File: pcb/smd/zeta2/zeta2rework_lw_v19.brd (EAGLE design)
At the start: 80.3 x 45.7 mm, 94 parts, among them IC1 MAX6520, U5 DS18B20U+

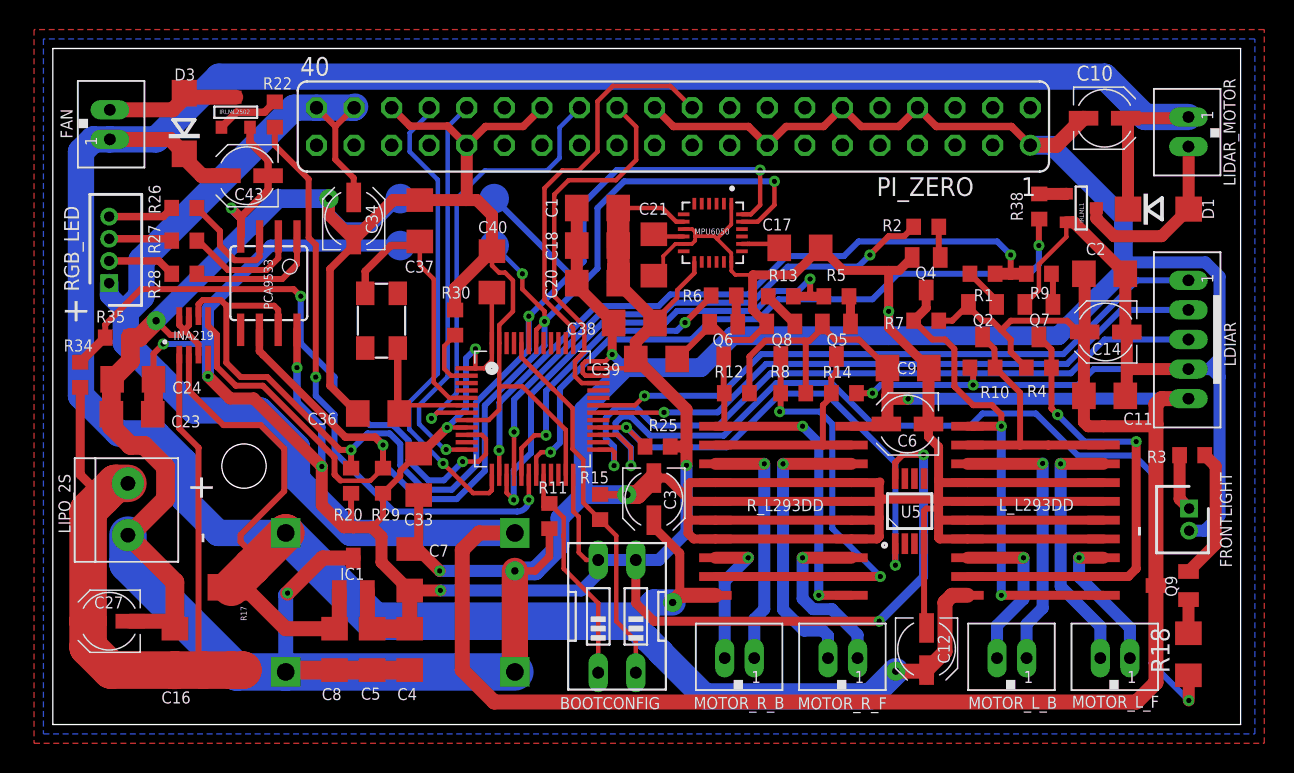
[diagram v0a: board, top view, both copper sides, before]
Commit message: using ph for leds again
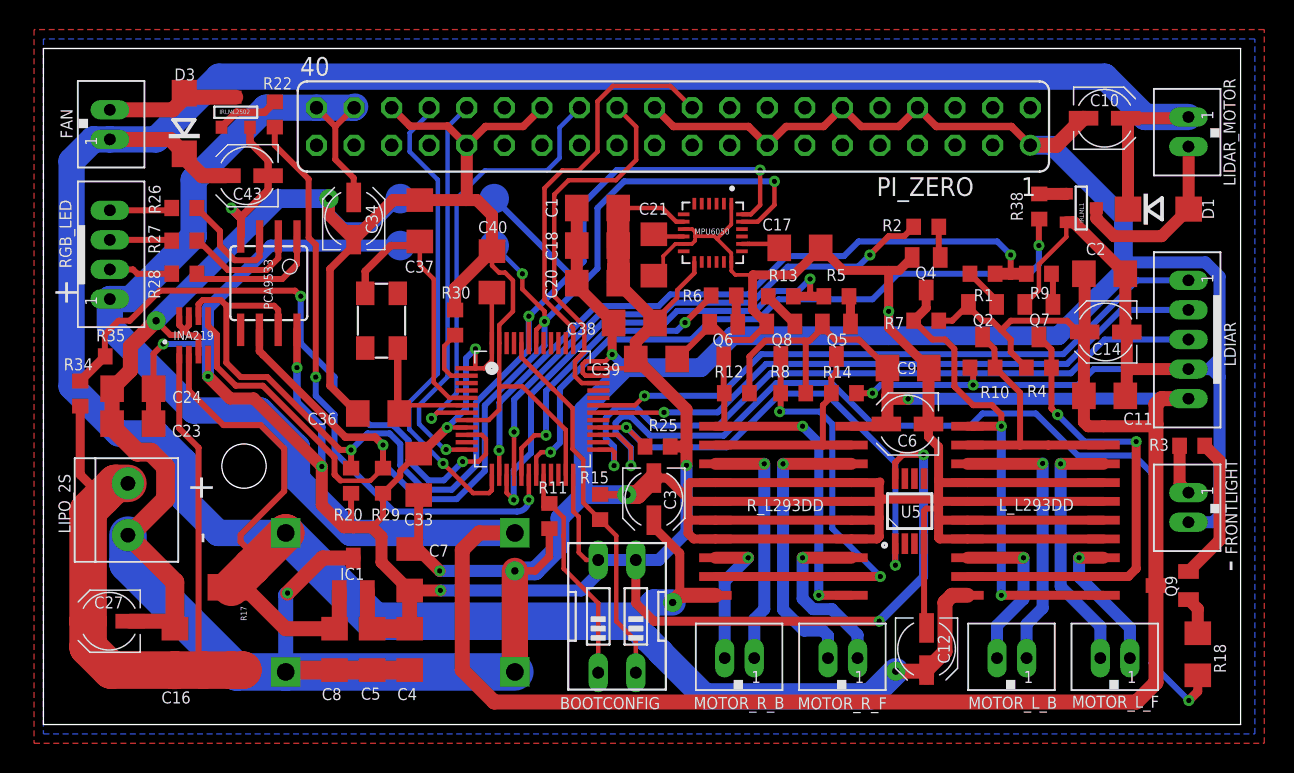
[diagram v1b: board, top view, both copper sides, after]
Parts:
- FRONTLIGHT: value B2B-ZR(LF)(SN) -> JST-PH_2-PIN_HEADER; device B2B-ZR(LF)(SN):SHDR2W50P0X150_1X2_450X350X450 -> srg:JST_B2B-PH_HEADER
- RGB_LED: value B4B-ZR(LF)(SN) -> JST-PH_4-PIN_HEADER; device B4B-ZR(LF)(SN):SHDR4W50P0X150_1X4_750X350X450 -> srg:JST_B4B-PH_HEADER
- moved RGB_LED 1.91 mm to (3.81, 38.7)
- moved R34 1.27 mm to (1.85, 29.4)
- moved R35 1.27 mm to (4.39, 31.9)
- moved C23 0.64 mm to (5.41, 27.3)
- moved R18 0.64 mm to (77.4, 11.7)
- moved C24 0.64 mm to (5.41, 29.7)
- moved R3 0.64 mm to (77.0, 25.8)
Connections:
- net +5V: now also RGB_LED.P1; no longer RGB_LED.1
- net GND: now also FRONTLIGHT.P2; no longer FRONTLIGHT.2
- net N$28: now also FRONTLIGHT.P1; no longer FRONTLIGHT.1
- net N$31: now also RGB_LED.P4; no longer RGB_LED.4
- net N$33: now also RGB_LED.P3; no longer RGB_LED.3
- net N$35: now also RGB_LED.P2; no longer RGB_LED.2
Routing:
- net V+: track 53.8 -> 52.6 mm
- net N$27: track 8.93 -> 9.78 mm
- net BAT_LVL: track 41.7 -> 42.5 mm
- net +3V3: track 199.8 -> 200.4 mm
- net +8V: track 239.0 -> 239.6 mm
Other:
- board size 80.3 x 45.7 mm -> 81 x 45.7 mm

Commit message: fixed power supply
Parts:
- removed LIPO_2S: TERMBLOCK_1X2-3.5MM, microbuilder:1X2-3.5MM
- added PWR: 691137710002, term block:691137710002
- R18: device rcl:R1206 -> rcl:R0603
- moved Q9 2.33 mm to (77.0, 14.4)
- moved C27 2.01 mm to (4.45, 12.1), turned to 270 degrees
- moved FRONTLIGHT 1.27 mm to (76.8, 20.3)
- moved R18 1.13 mm to (77.7, 10.6), turned to 0 degrees
- moved R3 0.72 mm to (77.0, 25.1)
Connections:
- net GND: now also PWR.2; no longer LIPO_2S.1
- net V+: now also PWR.1; no longer LIPO_2S.2
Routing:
- net GND: track 601.9 -> 597.8 mm
- net +5V: track 225.6 -> 226.9 mm
- net FRONT_LIGHT: track 67.1 -> 65.9 mm
- net N$20: track 9.78 -> 10.7 mm
- net V+: track 52.6 -> 53.3 mm
- net N$21: track 3.42 -> 4.01 mm
- net N$19: track 2.54 -> 3.05 mm
